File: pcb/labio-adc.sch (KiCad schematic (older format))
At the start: 5 parts

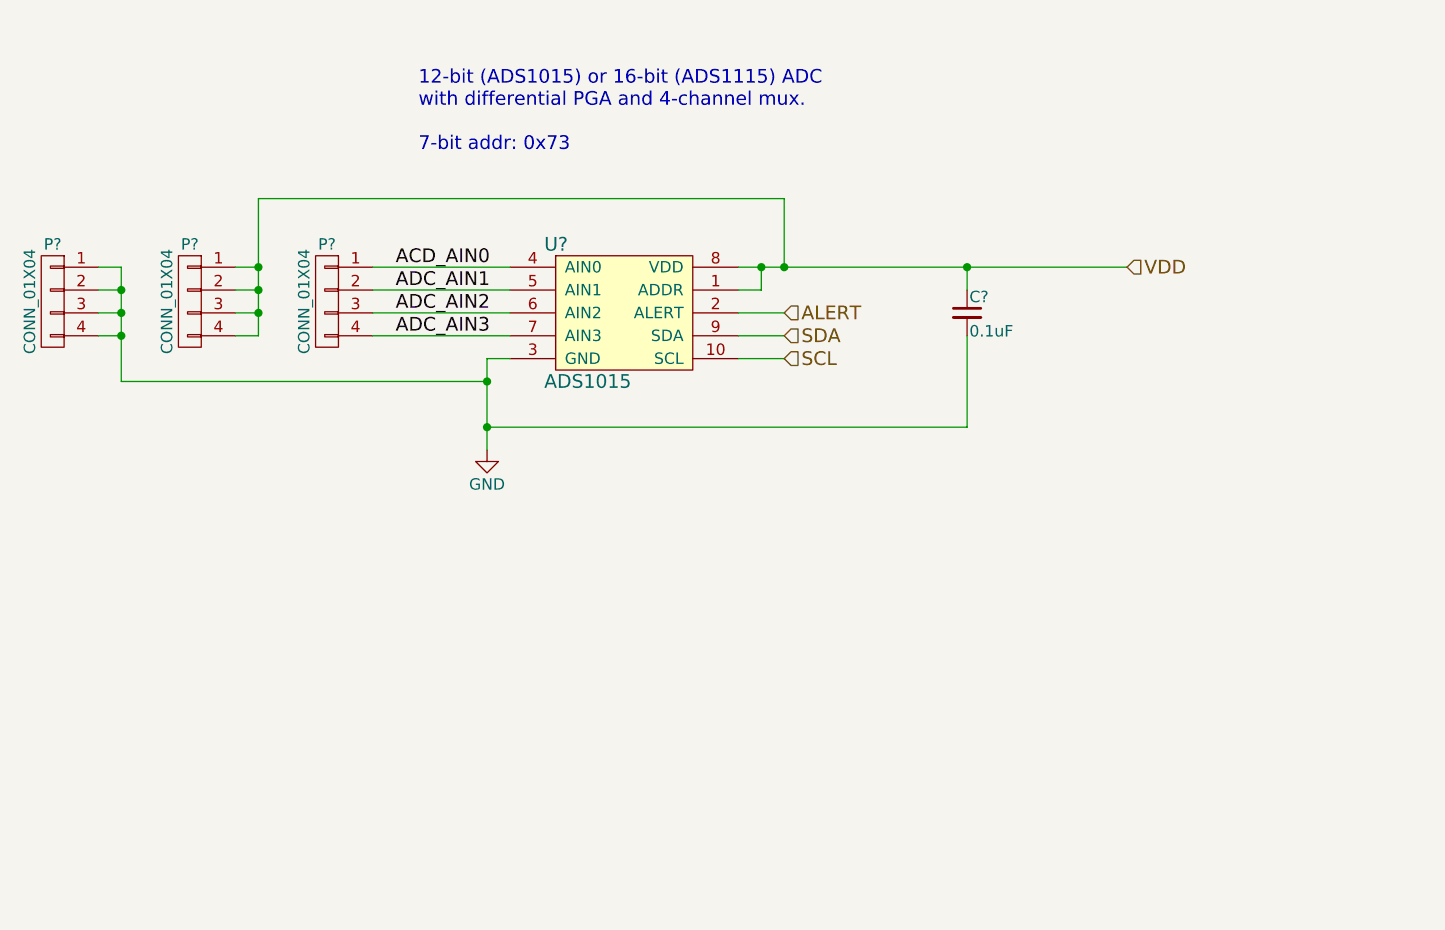
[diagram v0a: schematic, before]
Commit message: finish rpi to module connections
* use dip switches to disable/configure blocks
* add light sensor
* fix motor controller sense resistors
* fix overused jtag probe pins
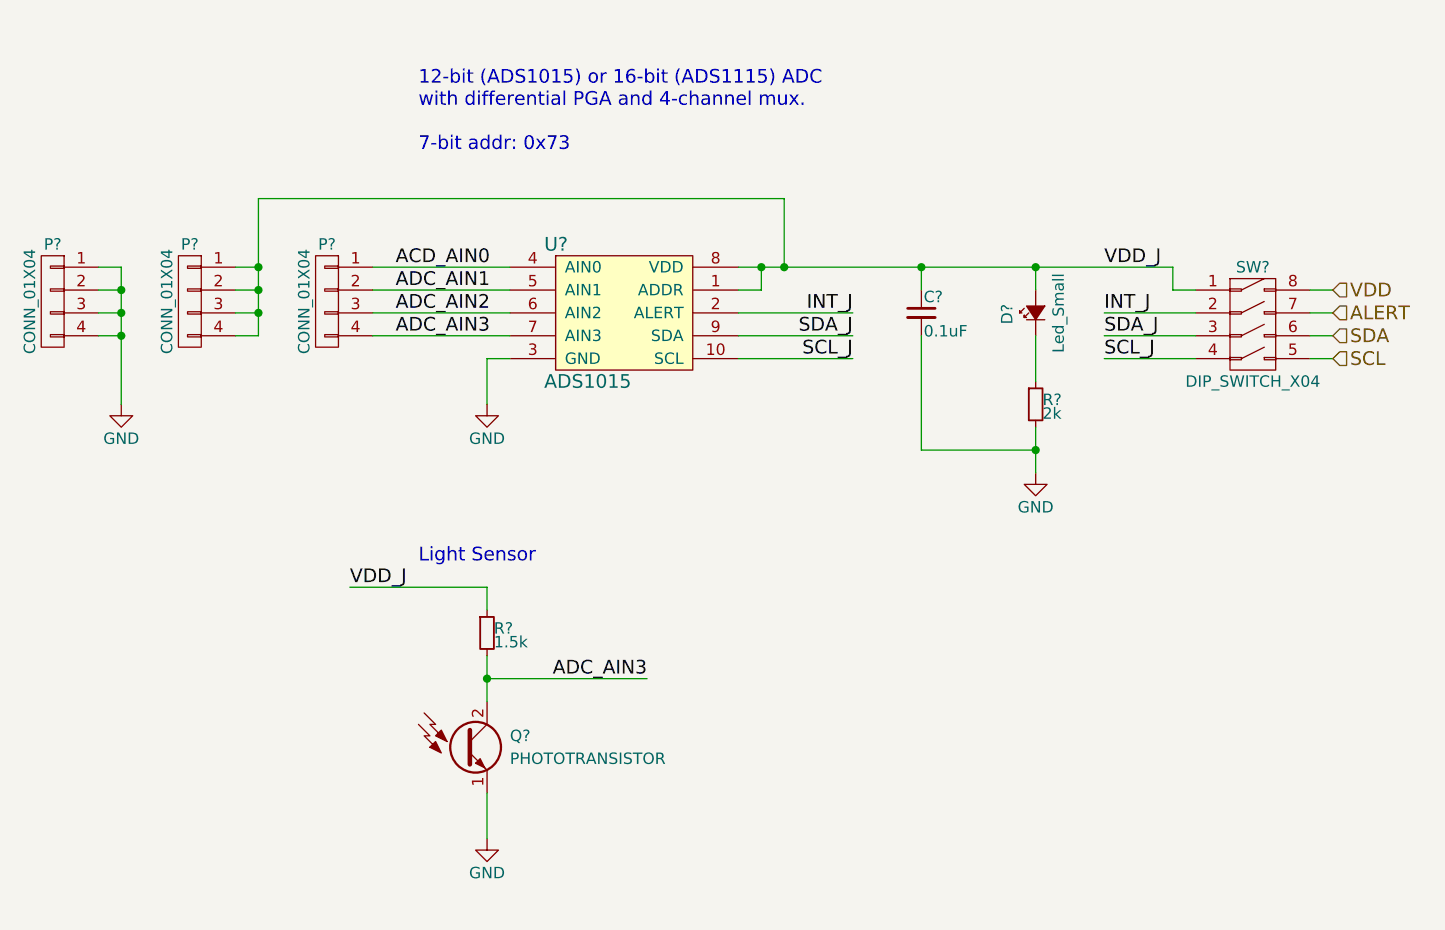
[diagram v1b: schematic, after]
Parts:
- added D?: Led_Small, symbol Led_Small
- added Q?: PHOTOTRANSISTOR, symbol PHOTOTRANSISTOR
- added R?: 1.5k, symbol R_Small
- added R?: 2k, symbol R_Small
- added SW?: DIP_SWITCH_X04, symbol DIP_SWITCH_X04
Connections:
- net ADC_AIN3: now also Q?.2 (C), R?.2
- net ALERT: now also SW?.7 (2A); no longer U?.2 (ALERT)
- net GND: now also Q?.1 (E), R?.2
- net SCL: now also SW?.5 (4B); no longer U?.10 (SCL)
- net SDA: now also SW?.6 (3B); no longer U?.9 (SDA)
- net VDD: now also SW?.8 (1B); no longer C?.1, P?.1 (P1), P?.2 (P2), P?.3 (P3), P?.4 (P4), U?.1 (ADDR), U?.8 (VDD)
- new net: D?.1 (K), R?.1
- new net INT_J: SW?.2 (2A), U?.2 (ALERT)
- new net SCL_J: SW?.4 (4A), U?.10 (SCL)
- new net SDA_J: SW?.3 (3A), U?.9 (SDA)
- new net VDD_J: C?.1, D?.2 (A), P?.1 (P1), P?.2 (P2), P?.3 (P3), P?.4 (P4), R?.1, SW?.1 (1A), U?.1 (ADDR), U?.8 (VDD)
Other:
- note added: "Light Sensor"
- moved on the sheet: C?
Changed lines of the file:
@@
 L GND #PWR?
 U 1 1 574C6823
-P 5700 4000
-F 0 "#PWR?" H 5700 3750 50  0001 C CNN
-F 1 "GND" H 5700 3850 50  0000 C CNN
-F 2 "" H 5700 4000 50  0000 C CNN
-F 3 "" H 5700 4000 50  0000 C CNN
-	1    5700 4000
+P 5700 3800
+F 0 "#PWR?" H 5700 3550 50  0001 C CNN
+F 1 "GND" H 5700 3650 50  0000 C CNN
+F 2 "" H 5700 3800 50  0000 C CNN
+F 3 "" H 5700 3800 50  0000 C CNN
+	1    5700 3800
 	1    0    0    -1
 $EndComp
@@
 L C_Small C?
 U 1 1 574C68FF
-P 7800 3400
-F 0 "C?" H 7810 3470 50  0000 L CNN
-F 1 "0.1uF" H 7810 3320 50  0000 L CNN
-F 2 "" H 7800 3400 50  0000 C CNN
-F 3 "" H 7800 3400 50  0000 C CNN
-	1    7800 3400
-	1    0    0    -1
-$EndComp
-Text HLabel 8500 3200 2    60   Input ~ 0
+P 7600 3400
+F 0 "C?" H 7610 3470 50  0000 L CNN
+F 1 "0.1uF" H 7610 3320 50  0000 L CNN
+F 2 "" H 7600 3400 50  0000 C CNN
+F 3 "" H 7600 3400 50  0000 C CNN
+	1    7600 3400
+	1    0    0    -1
+$EndComp
+Text HLabel 9400 3300 2    60   Input ~ 0
 VDD
-Text HLabel 7000 3500 2    60   Input ~ 0
+Text HLabel 9400 3500 2    60   Input ~ 0
 SDA
-Text HLabel 7000 3600 2    60   Input ~ 0
+Text HLabel 9400 3600 2    60   Input ~ 0
 SCL
-Text HLabel 7000 3400 2    60   Input ~ 0
+Text HLabel 9400 3400 2    60   Input ~ 0
 ALERT
 Wire Wire Line
-	8500 3200 6800 3200
-Wire Wire Line
-	6800 3400 7000 3400
-Wire Wire Line
-	7000 3500 6800 3500
-Wire Wire Line
-	6800 3600 7000 3600
+	6800 3400 7300 3400
+Wire Wire Line
+	7300 3500 6800 3500
+Wire Wire Line
+	6800 3600 7300 3600
 Wire Wire Line
 	5200 3200 5800 3200
@@
 	5200 3400 5800 3400
 Wire Wire Line
-	5800 3500 5200 3500
-Wire Wire Line
-	5700 4000 5700 3600
-Wire Wire Line
 	5700 3600 5800 3600
 Wire Wire Line
-	5700 3700 4100 3700
-Wire Wire Line
-	4100 3700 4100 3200
+	4100 3200 4100 3300
+Wire Wire Line
+	4100 3300 4100 3400
+Wire Wire Line
+	4100 3400 4100 3500
+Wire Wire Line
+	4100 3500 4100 3800
 Wire Wire Line
 	4100 3200 4000 3200
-Connection ~ 5700 3700
 Wire Wire Line
 	4000 3300 4100 3300
@@
 Connection ~ 4100 3500
 Wire Wire Line
-	4600 3500 4700 3500
-Wire Wire Line
-	4700 3500 4700 2900
+	4700 3500 4600 3500
+Wire Wire Line
+	4700 2900 4700 3200
+Wire Wire Line
+	4700 3200 4700 3300
+Wire Wire Line
+	4700 3300 4700 3400
+Wire Wire Line
+	4700 3400 4700 3500
 Wire Wire Line
 	4700 2900 7000 2900
-Wire Wire Line
-	7000 2900 7000 3200
-Connection ~ 7000 3200
 Wire Wire Line
 	4600 3400 4700 3400
@@
 Connection ~ 4700 3200
 Wire Wire Line
-	5700 3900 7800 3900
-Wire Wire Line
-	7800 3900 7800 3500
-Connection ~ 5700 3900
-Wire Wire Line
-	7800 3300 7800 3200
-Connection ~ 7800 3200
-Wire Wire Line
 	6800 3300 6900 3300
-Wire Wire Line
-	6900 3300 6900 3200
-Connection ~ 6900 3200
 Text Notes 5400 2700 0    60   ~ 0
 12-bit (ADS1015) or 16-bit (ADS1115) ADC\nwith differential PGA and 4-channel mux.\n\n7-bit addr: 0x73
@@
 Text Label 5300 3500 0    60   ~ 0
 ADC_AIN3
+Wire Wire Line
+	5200 3500 5800 3500
+$Comp
+L PHOTOTRANSISTOR Q?
+U 1 1 576D542D
+P 5600 5300
+F 0 "Q?" H 5800 5350 50  0000 L CNN
+F 1 "PHOTOTRANSISTOR" H 5800 5250 50  0000 L CNN
+F 2 "" H 5800 5400 50  0000 C CNN
+F 3 "" H 5600 5300 50  0000 C CNN
+	1    5600 5300
+	1    0    0    -1
+$EndComp
+$Comp
+L GND #PWR?
+U 1 1 576D549A
+P 5700 5700
+F 0 "#PWR?" H 5700 5450 50  0001 C CNN
+F 1 "GND" H 5700 5550 50  0000 C CNN
+F 2 "" H 5700 5700 50  0000 C CNN
+F 3 "" H 5700 5700 50  0000 C CNN
+	1    5700 5700
+	1    0    0    -1
+$EndComp
+$Comp
+L R_Small R?
+U 1 1 576D54B9
+P 5700 4800
+F 0 "R?" H 5730 4820 50  0000 L CNN
+F 1 "1.5k" H 5730 4760 50  0000 L CNN
+F 2 "" H 5700 4800 50  0000 C CNN
+F 3 "" H 5700 4800 50  0000 C CNN
+	1    5700 4800
+	1    0    0    -1
+$EndComp
+Wire Wire Line
+	5700 4700 5700 4600
+Wire Wire Line
+	5700 4600 5100 4600
+Wire Wire Line
+	5700 4900 5700 5000
+Wire Wire Line
+	5700 5000 5700 5100
+Wire Wire Line
+	5700 5000 6400 5000
+Connection ~ 5700 5000
+Wire Wire Line
+	5700 5500 5700 5700
+Text Notes 5400 4500 0    60   ~ 0
+Light Sensor
+Text Label 6400 5000 2    60   ~ 0
+ADC_AIN3
+$Comp
+L DIP_SWITCH_X04 SW?
+U 1 1 576D562D
+P 9050 3450
+F 0 "SW?" H 9050 3700 50  0000 C CNN
+F 1 "DIP_SWITCH_X04" H 9050 3200 50  0000 C CNN
+F 2 "" H 9050 2250 50  0000 C CNN
+F 3 "" H 9050 2250 50  0000 C CNN
+	1    9050 3450
+	1    0    0    -1
+$EndComp
+$Comp
+L Led_Small D?
+U 1 1 576D57C2
+P 8100 3400
+F 0 "D?" H 8050 3525 50  0000 L CNN
+F 1 "Led_Small" H 7925 3300 50  0000 L CNN
+F 2 "" V 8100 3400 50  0000 C CNN
+F 3 "" V 8100 3400 50  0000 C CNN
+	1    8100 3400
+	0    -1   -1   0
+$EndComp
+$Comp
+L R_Small R?
+U 1 1 576D5877
+P 8100 3800
+F 0 "R?" H 8130 3820 50  0000 L CNN
+F 1 "2k" H 8130 3760 50  0000 L CNN
+F 2 "" H 8100 3800 50  0000 C CNN
+F 3 "" H 8100 3800 50  0000 C CNN
+	1    8100 3800
+	1    0    0    -1
+$EndComp
+Wire Wire Line
+	5700 3800 5700 3600
+$Comp
+L GND #PWR?
+U 1 1 576D595B
+P 4100 3800
+F 0 "#PWR?" H 4100 3550 50  0001 C CNN
+F 1 "GND" H 4100 3650 50  0000 C CNN
+F 2 "" H 4100 3800 50  0000 C CNN
+F 3 "" H 4100 3800 50  0000 C CNN
+	1    4100 3800
+	1    0    0    -1
+$EndComp
+$Comp
+L GND #PWR?
+U 1 1 576D5995
+P 8100 4100
+F 0 "#PWR?" H 8100 3850 50  0001 C CNN
+F 1 "GND" H 8100 3950 50  0000 C CNN
+F 2 "" H 8100 4100 50  0000 C CNN
+F 3 "" H 8100 4100 50  0000 C CNN
+	1    8100 4100
+	1    0    0    -1
+$EndComp
+Wire Wire Line
+	8100 3900 8100 4000
+Wire Wire Line
+	8100 4000 8100 4100
+Wire Wire Line
+	8100 4000 7600 4000
+Wire Wire Line
+	7600 4000 7600 3500
+Connection ~ 8100 4000
+Wire Wire Line
+	8100 3500 8100 3700
+Wire Wire Line
+	8800 3400 8400 3400
+Wire Wire Line
+	8400 3500 8800 3500
+Wire Wire Line
+	8800 3600 8400 3600
+Wire Wire Line
+	8800 3300 8700 3300
+Wire Wire Line
+	8700 3300 8700 3200
+Wire Wire Line
+	8700 3200 8100 3200
+Wire Wire Line
+	8100 3200 7600 3200
+Wire Wire Line
+	7600 3200 7000 3200
+Wire Wire Line
+	7000 3200 6900 3200
+Wire Wire Line
+	6900 3200 6800 3200
+Wire Wire Line
+	6900 3300 6900 3200
+Connection ~ 6900 3200
+Wire Wire Line
+	7000 2900 7000 3200
+Connection ~ 7000 3200
+Wire Wire Line
+	7600 3300 7600 3200
+Connection ~ 7600 3200
+Wire Wire Line
+	8100 3300 8100 3200
+Connection ~ 8100 3200
+Wire Wire Line
+	9400 3300 9300 3300
+Wire Wire Line
+	9300 3400 9400 3400
+Wire Wire Line
+	9400 3500 9300 3500
+Wire Wire Line
+	9300 3600 9400 3600
+Text Label 8400 3200 0    60   ~ 0
+VDD_J
+Text Label 8400 3400 0    60   ~ 0
+INT_J
+Text Label 8400 3500 0    60   ~ 0
+SDA_J
+Text Label 8400 3600 0    60   ~ 0
+SCL_J
+Text Label 7300 3400 2    60   ~ 0
+INT_J
+Text Label 7300 3500 2    60   ~ 0
+SDA_J
+Text Label 7300 3600 2    60   ~ 0
+SCL_J
+Text Label 5100 4600 0    60   ~ 0
+VDD_J
 $EndSCHEMATC
